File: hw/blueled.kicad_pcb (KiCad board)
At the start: 2 copper layers, 26 x 61.7 mm, 23 parts, among them J1 Barrel_Jack, J2 Screw_Terminal_01x03, J3 ICSP, Q1 Q_PMOS_SDG, SW1 SW_Push_SPDT, SW2 PUSH, U1 ATmega328P-AU, U2 HC-05, U3 LM1117-3.3, U4 AT25DF512x-UxN-x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

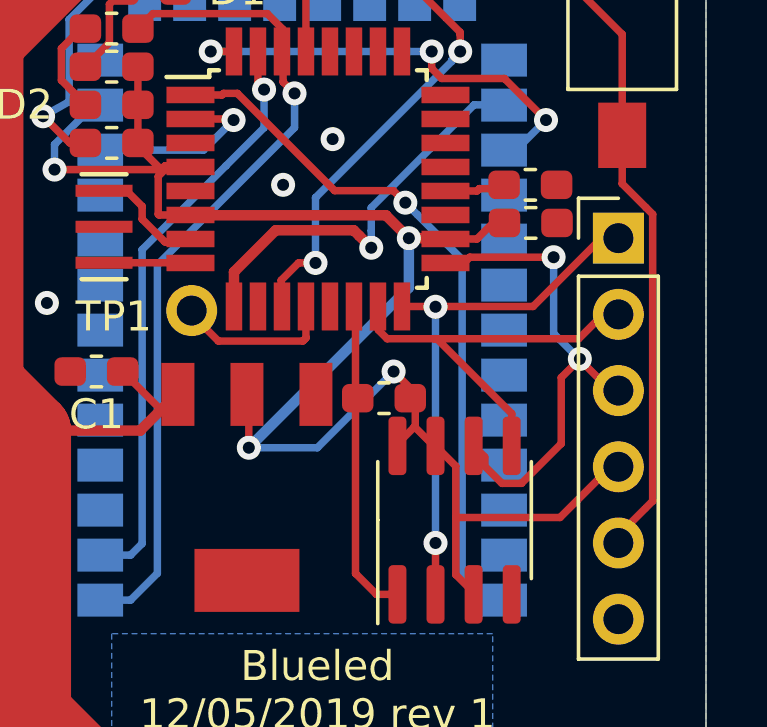
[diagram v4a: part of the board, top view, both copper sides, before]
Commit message: HW: Remove big pads for MOSFET
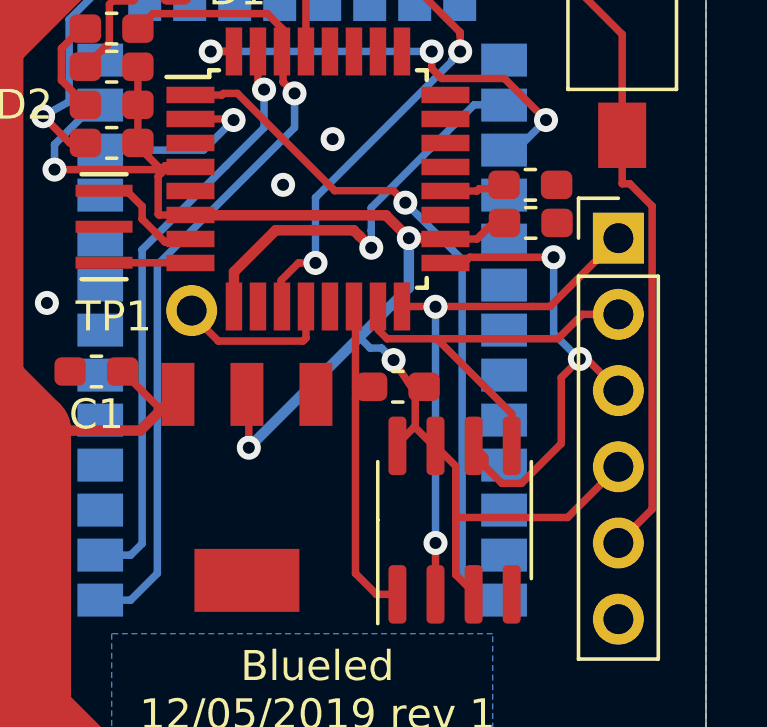
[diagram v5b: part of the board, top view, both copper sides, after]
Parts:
- moved R4 0.60 mm to (156.1, 121.2)
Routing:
- net +3V3: track 55.5 -> 51.7 mm
- net MISO: track 17.5 -> 18.1 mm
- net FLASH_CSN: track 10.4 -> 11.0 mm

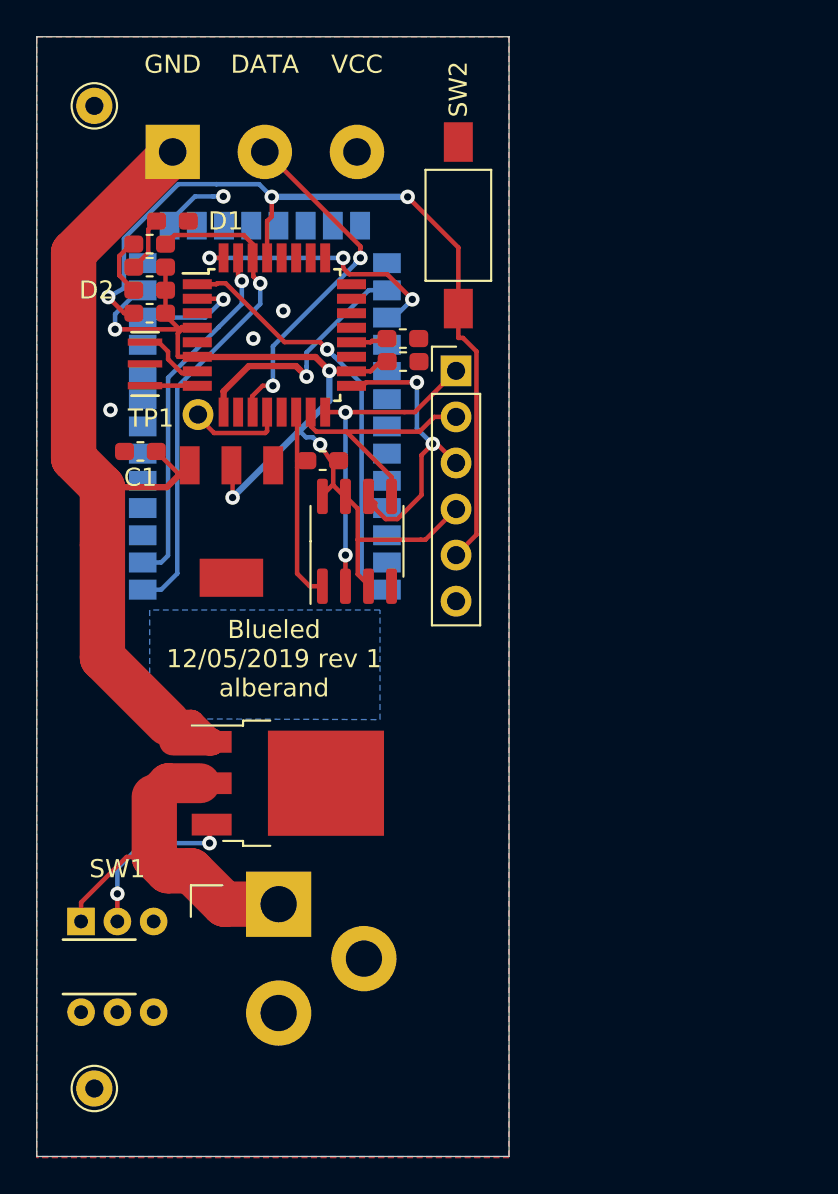
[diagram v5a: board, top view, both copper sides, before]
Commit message: Add region for VIN
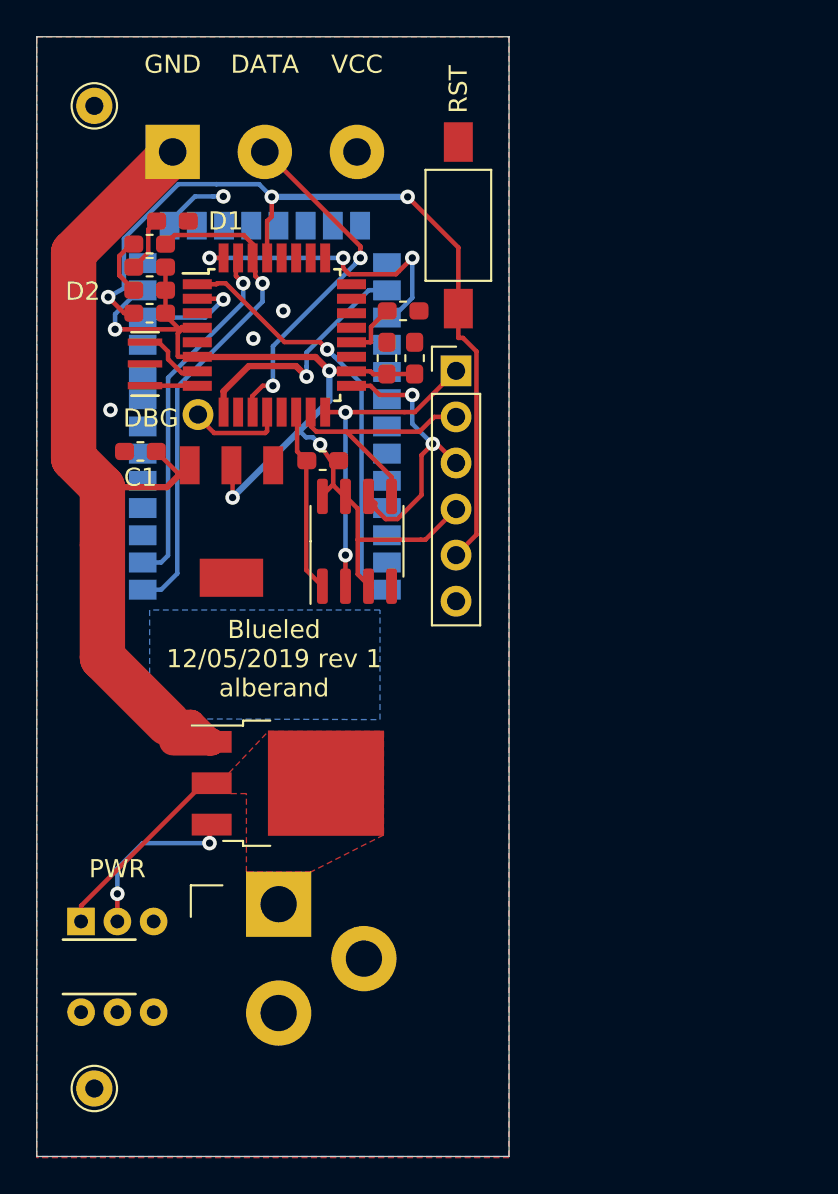
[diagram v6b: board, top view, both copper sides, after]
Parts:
- added C4: 100n, Capacitor_SMD:C_0603_1608Metric_Pad1.05x0.95mm_HandSolder, F.Cu at (159.6, 115.5)
- moved C3 1.52 mm to (160.5, 112.9)
- moved C2 0.66 mm to (161.2, 115.5), turned to 90 degrees
- renumbered TP1 to DBG, SW1 to PWR, SW2 to RST
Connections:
- Q1 pad 4: (no net) -> /VINJACK
- U3 pad 4: (no net) -> +3V3
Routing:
- net /VINJACK: track 20.2 -> 10.8 mm
- net HC-STATE: track 15.3 -> 17.4 mm
- net +3V3: track 51.7 -> 53.2 mm
- net Net-(C3-Pad1): track 1.61 -> 3.15 mm
- net FLASH_CSN: track 11.0 -> 9.72 mm
- added copper zone on F.Cu, net /VINJACK

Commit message: Minor updates
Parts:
- renumbered U2 to HC-05
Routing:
- net GND: track 3.81 -> 5.64 mm
- net VIN: track 48.0 -> 47.1 mm
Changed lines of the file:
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@@
   )
   (setup
-    (last_trace_width 0.25)
+    (last_trace_width 2.5)
     (user_trace_width 0.35)
     (user_trace_width 1.5)
@@
     (solder_mask_min_width 0.25)
     (aux_axis_origin 0 0)
+    (grid_origin 149.987 136.652)
     (visible_elements FFFFFF7F)
     (pcbplotparams
@@
     (tags "hc-05, bluetooth")
     (attr smd)
-    (fp_text reference U2 (at 0 0) (layer B.SilkS)
+    (fp_text reference HC-05 (at 0 0) (layer B.SilkS)
       (effects (font (size 1 1) (thickness 0.15)) (justify mirror))
     )
@@
   (segment (start 147.658 108.204) (end 147.658 107.992) (width 0.25) (layer B.Cu) (net 43))
   (segment (start 159.5838 114.681) (end 159.639 114.681) (width 0.25) (layer F.Cu) (net 43))
-  (segment (start 149.978 136.658) (end 147.834 136.658) (width 1.5) (layer F.Cu) (net 44))
-  (segment (start 147.574 135.636) (end 143.953999 132.015999) (width 2.5) (layer F.Cu) (net 44))
-  (segment (start 143.953999 132.015999) (end 143.953999 125.794001) (width 2.5) (layer F.Cu) (net 44))
-  (segment (start 149.978 136.658) (end 149.866 136.658) (width 1.5) (layer F.Cu) (net 44))
-  (segment (start 149.866 136.658) (end 148.844 135.636) (width 1.5) (layer F.Cu) (net 44))
-  (segment (start 148.844 135.636) (end 147.574 135.636) (width 1.5) (layer F.Cu) (net 44))
-  (segment (start 143.953999 125.794001) (end 143.953999 122.617999) (width 2.5) (layer F.Cu) (net 44))
+  (segment (start 161.163 114.0065) (end 161.417 113.7525) (width 0.25) (layer F.Cu) (net 43))
+  (segment (start 161.163 114.6315) (end 161.163 114.0065) (width 0.25) (layer F.Cu) (net 43))
+  (segment (start 161.417 113.7525) (end 161.417 112.903) (width 0.25) (layer F.Cu) (net 43))
   (segment (start 143.953999 122.617999) (end 147.511001 122.617999) (width 0.35) (layer F.Cu) (net 44))
   (segment (start 147.511001 122.617999) (end 148.209 121.92) (width 0.35) (layer F.Cu) (net 44))
@@
   (segment (start 142.367 109.681208) (end 142.367 121.031) (width 2.5) (layer F.Cu) (net 44))
   (segment (start 147.701 104.347208) (end 142.367 109.681208) (width 2.5) (layer F.Cu) (net 44))
+  (segment (start 143.953999 125.794001) (end 143.953999 122.617999) (width 2.5) (layer F.Cu) (net 44))
+  (segment (start 143.953999 134.233999) (end 143.953999 125.794001) (width 2.5) (layer F.Cu) (net 44))
+  (segment (start 146.378 136.658) (end 143.953999 134.233999) (width 2.5) (layer F.Cu) (net 44))
+  (segment (start 149.978 136.658) (end 146.378 136.658) (width 2.5) (layer F.Cu) (net 44))
   (segment (start 144.88299 110.93979) (end 145.5762 111.633) (width 0.25) (layer F.Cu) (net 45))
   (segment (start 144.88299 110.93979) (end 144.88299 109.87901) (width 0.25) (layer F.Cu) (net 45))
@@
     (polygon
       (pts
-        (xy 146.558 129.286) (xy 159.258 129.286) (xy 159.258 135.382) (xy 146.558 135.382)
+        (xy 146.558 134.874) (xy 146.558 129.286) (xy 159.258 129.286) (xy 159.258 135.382) (xy 146.939 135.382)
       )
     )

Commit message: Rev 0.1
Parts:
- removed C4: 100n, Capacitor_SMD:C_0603_1608Metric_Pad1.05x0.95mm_HandSolder
- moved Debug Handler 1.14 mm to (142.4, 101.6)
- moved REF** 1.14 mm to (142.4, 155.8)
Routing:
- net +3V3: track 53.2 -> 65.7 mm, vias 4 -> 5
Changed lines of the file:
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@@
     (thickness 1.6)
     (drawings 5)
-    (tracks 244)
+    (tracks 250)
     (zones 0)
-    (modules 24)
+    (modules 23)
     (nets 57)
   )
@@
   )
   (setup
-    (last_trace_width 2.5)
+    (last_trace_width 0.35)
     (user_trace_width 0.35)
     (user_trace_width 1.5)
@@
     (visible_elements FFFFFF7F)
     (pcbplotparams
-      (layerselection 0x010fc_ffffffff)
+      (layerselection 0x010f0_ffffffff)
       (usegerberextensions false)
       (usegerberattributes false)
@@
       (outputformat 1)
       (mirror false)
-      (drillshape 1)
+      (drillshape 0)
       (scaleselection 1)
-      (outputdirectory ""))
+      (outputdirectory "/home/andrew/Projects/blueled/hw/manufacturing/"))
   )
   (net 0 "")
@@
     (add_net VIN)
   )
-  (module Capacitor_SMD:C_0603_1608Metric_Pad1.05x0.95mm_HandSolder (layer F.Cu)
-    (at 159.639 115.5065 90)
-    (descr "Capacitor SMD 0603 (1608 Metric), square (rectangular) end terminal, IPC_7351 nominal with elongated pad for handsoldering. (Body size source: http://www.tortai-tech.com/upload/download/2011102023233369053.pdf), generated with kicad-footprint-generator")
-    (tags "capacitor handsolder")
-    (attr smd)
-    (fp_text reference C4 (at 0 -1.43 90) (layer F.SilkS) hide
-      (effects (font (size 1 1) (thickness 0.15)))
-    )
-    (fp_text value 100n (at 0 1.43 90) (layer F.Fab)
-      (effects (font (size 1 1) (thickness 0.15)))
-    )
-    (fp_text user %R (at 0 0 90) (layer F.Fab)
-      (effects (font (size 0.4 0.4) (thickness 0.06)))
-    )
-    (fp_line (start 1.65 0.73) (end -1.65 0.73) (layer F.CrtYd) (width 0.05))
-    (fp_line (start 1.65 -0.73) (end 1.65 0.73) (layer F.CrtYd) (width 0.05))
-    (fp_line (start -1.65 -0.73) (end 1.65 -0.73) (layer F.CrtYd) (width 0.05))
-    (fp_line (start -1.65 0.73) (end -1.65 -0.73) (layer F.CrtYd) (width 0.05))
-    (fp_line (start -0.171267 0.51) (end 0.171267 0.51) (layer F.SilkS) (width 0.12))
-    (fp_line (start -0.171267 -0.51) (end 0.171267 -0.51) (layer F.SilkS) (width 0.12))
-    (fp_line (start 0.8 0.4) (end -0.8 0.4) (layer F.Fab) (width 0.1))
-    (fp_line (start 0.8 -0.4) (end 0.8 0.4) (layer F.Fab) (width 0.1))
-    (fp_line (start -0.8 -0.4) (end 0.8 -0.4) (layer F.Fab) (width 0.1))
-    (fp_line (start -0.8 0.4) (end -0.8 -0.4) (layer F.Fab) (width 0.1))
-    (pad 2 smd roundrect (at 0.875 0 90) (size 1.05 0.95) (layers F.Cu F.Paste F.Mask) (roundrect_rratio 0.25)
-      (net 43 GND))
-    (pad 1 smd roundrect (at -0.875 0 90) (size 1.05 0.95) (layers F.Cu F.Paste F.Mask) (roundrect_rratio 0.25)
-      (net 1 +3V3))
-    (model ${KISYS3DMOD}/Capacitor_SMD.3dshapes/C_0603_1608Metric.wrl
-      (at (xyz 0 0 0))
-      (scale (xyz 1 1 1))
-      (rotate (xyz 0 0 0))
-    )
-  )
   (module LED_SMD:LED_0603_1608Metric_Pad1.05x0.95mm_HandSolder (layer F.Cu)
     (at 147.814 107.95 180)
@@
   )
   (module Connector_Pin:Pin_D1.0mm_L10.0mm (layer F.Cu)
-    (at 143.51 101.6)
+    (at 142.367 101.6)
     (descr "solder Pin_ diameter 1.0mm, hole diameter 1.0mm (press fit), length 10.0mm")
     (tags "solder Pin_ press fit")
@@
   )
   (module Connector_Pin:Pin_D1.0mm_L10.0mm (layer F.Cu)
-    (at 143.51 155.7655)
+    (at 142.367 155.7655)
     (descr "solder Pin_ diameter 1.0mm, hole diameter 1.0mm (press fit), length 10.0mm")
     (tags "solder Pin_ press fit")
@@
   (segment (start 156.464 116.259879) (end 156.464 116.205) (width 0.35) (layer B.Cu) (net 1))
   (segment (start 156.464 117.856) (end 156.464 116.259879) (width 0.35) (layer B.Cu) (net 1))
-  (segment (start 155.702 115.443) (end 149.606 115.443) (width 0.35) (layer F.Cu) (net 1))
   (segment (start 156.464 116.205) (end 157.099 116.205) (width 0.35) (layer F.Cu) (net 1))
   (segment (start 148.209 113.919) (end 148.336 113.792) (width 0.25) (layer F.Cu) (net 1))
@@
   (segment (start 158.8983 116.3955) (end 159.639 116.3955) (width 0.25) (layer F.Cu) (net 1))
   (segment (start 159.639 116.3815) (end 161.022 116.3815) (width 0.25) (layer F.Cu) (net 1))
+  (segment (start 151.0665 123.2535) (end 151.13 123.19) (width 0.25) (layer F.Cu) (net 1))
+  (segment (start 151.0665 127.612) (end 151.0665 123.2535) (width 0.25) (layer F.Cu) (net 1))
+  (segment (start 151.13 123.19) (end 151.13 115.443) (width 0.25) (layer B.Cu) (net 1))
+  (segment (start 151.13 115.443) (end 150.876 115.443) (width 0.25) (layer B.Cu) (net 1))
+  (via (at 150.876 115.443) (size 0.8) (drill 0.4) (layers F.Cu B.Cu) (net 1))
+  (segment (start 155.702 115.443) (end 150.876 115.443) (width 0.35) (layer F.Cu) (net 1))
+  (segment (start 150.876 115.443) (end 149.606 115.443) (width 0.35) (layer F.Cu) (net 1))
   (segment (start 157.6848 114.632) (end 158.7348 114.632) (width 0.25) (layer F.Cu) (net 2))
   (segment (start 158.7348 114.632) (end 158.759801 114.606999) (width 0.25) (layer F.Cu) (net 2))
